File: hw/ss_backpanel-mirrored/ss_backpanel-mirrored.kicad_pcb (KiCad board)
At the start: 2 copper layers, 165 x 51.1 mm, 17 parts, among them J101 4mm_banana_socket-LB_I4R_A-pa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, M101 Amphenol_T3437000-DIN7_panel_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, M102 Amphenol_T3437000-DIN7_panel_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, M103 Mech_cutout_IDC_2x5, M104 FN283-1-06_Schaffner_AC-panel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, M105 74980104400-Wurth_RJ45-Panel_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, M106 TE-1734346-Panel_cutout, M107 CUI-UJ2_AH_1_SMT-Panel_cutout, M109 SJ-3571N_CUI_audio_jacket_pan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, M110 SMA_bulkhead_jack_Panel_cutout, M111 Molex_NanoFit-1x02-Panel_cuto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

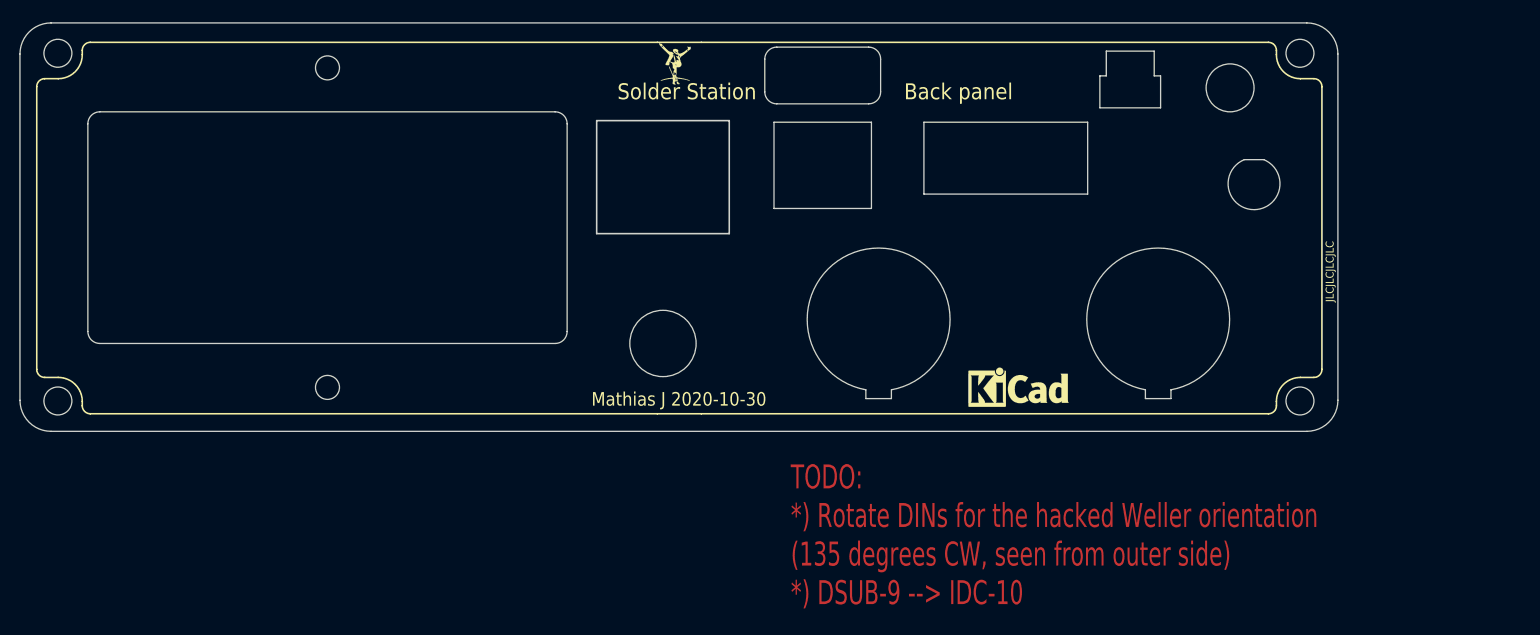
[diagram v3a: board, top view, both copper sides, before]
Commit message: Yet another rear-panel layout shuffle : audio-out to other side; adjust Eth & debug-IDC; align & cleanup
Moving the audio-conn might help confining the audio parts to the rear-right side of MB.
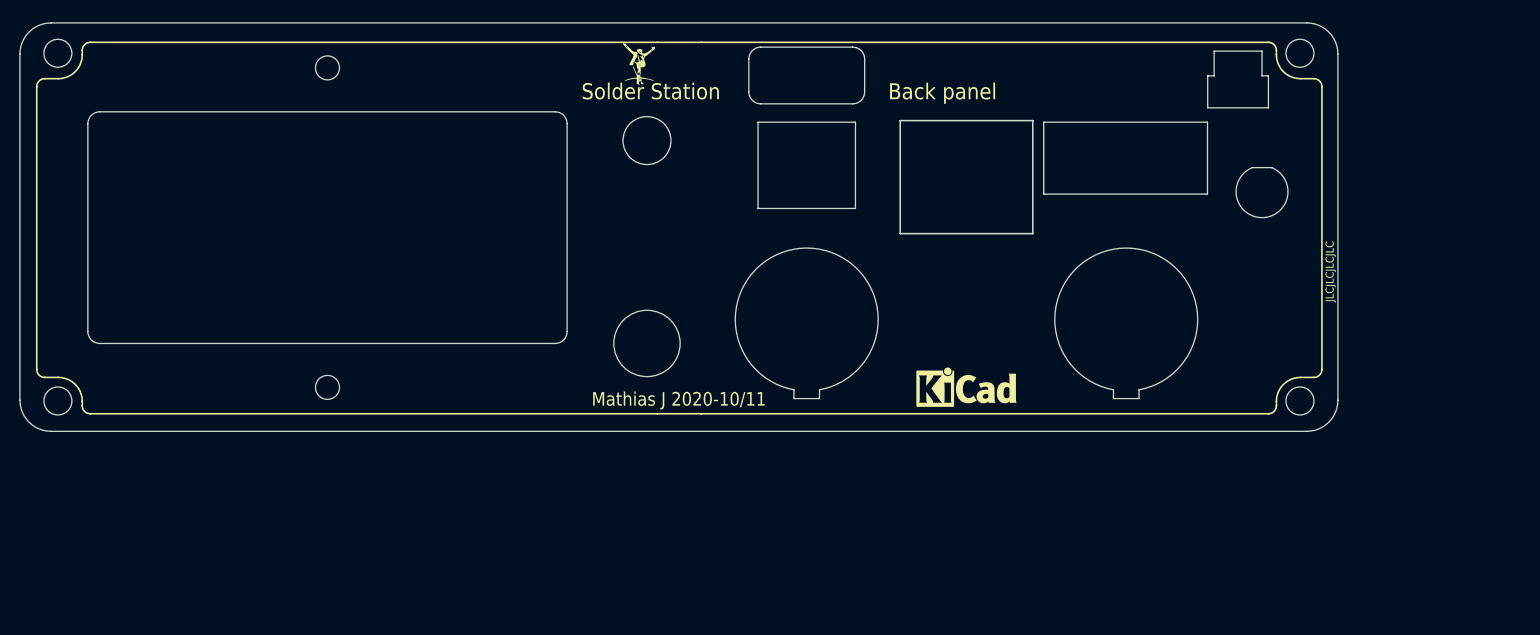
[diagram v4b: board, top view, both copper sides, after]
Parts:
- moved M109 73.0 mm to (146.0, 61.1), turned to 0 degrees
- moved M105 38.0 mm to (186.0, 61.1)
- moved M103 15.0 mm to (205.9, 61.3)
- moved M111 13.5 mm to (220.0, 59.5)
- moved M102 9.00 mm to (166.0, 86.0)
- moved LOGO101 6.50 mm to (186.0, 95.0)
- moved Logo103 4.50 mm to (145.0, 54.0)
- moved M101 4.00 mm to (206.0, 86.0)
- moved J101 2.00 mm to (146.0, 89.0)
- moved M106 2.00 mm to (166.0, 61.1)
- moved M107 2.00 mm to (166.0, 59.5)
- moved M110 1.41 mm to (223.0, 70.0)
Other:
- board text added: "Mathias J 2020-10/11"
- board text removed: "Mathias J 2020-10-30"
- board text removed: "TODO: *) Rotate DINs for the hacked Weller orientation (135 degrees CW, seen from outer side) *) DSUB-9 --> IDC-10"
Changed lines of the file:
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@@
-(kicad_pcb (version 20171130) (host pcbnew 5.1.7-a382d34a8~87~ubuntu18.04.1)
+(kicad_pcb (version 20171130) (host pcbnew 5.1.8-db9833491~87~ubuntu18.04.1)
   (general
     (thickness 1.6)
-    (drawings 49)
+    (drawings 48)
     (tracks 0)
     (zones 0)
@@
   )
   (module customlib_mj_fp:Mech_cutout_IDC_2x5 locked (layer F.Cu)
-    (at 190.92 61.3 180)
+    (at 205.92 61.3 180)
     (descr "Panel cut-out for a right-angled IDC 2x5")
     (tags "IDC 2x5")
@@
   )
   (module customlib_mj_fp:Molex_NanoFit-1x02-Panel_cutout locked (layer B.Cu)
-    (at 206.5 59.5 180)
+    (at 220 59.5 180)
     (descr "Panel cut-out for Molex Nano-Fit 1x02")
     (tags "Molex NanoFit panel cut-out")
@@
     )
   )
-  (module customlib_mj_fp:SMA_Bulkhead_jack-Panel_cutout (layer B.Cu)
-    (at 222 69 90)
+  (module customlib_mj_fp:SMA_Bulkhead_jack-Panel_cutout locked (layer B.Cu)
+    (at 223 70 90)
     (descr "SMA bulkhead jack connector cut-out")
     (tags "SMA panel cutout")
@@
   )
   (module customlib_mj_fp:LB_I4R_A-4mm_banana_socket_panelmnt locked (layer B.Cu)
-    (at 148 89 180)
+    (at 146 89 180)
     (fp_text reference J101 (at 0 5) (layer B.SilkS) hide
       (effects (font (size 1.2 0.8) (thickness 0.16)) (justify mirror))
@@
   )
   (module customlib_mj_fp:CUI-UJ2_AH_1_SMT-Panel_cutout locked (layer B.Cu)
-    (at 168 59.5 180)
+    (at 166 59.5 180)
     (descr "Panel cut-out for CUI-UJ2_AH_1_SMT USB-A host connector")
     (tags "USB-A CUI UJ2_AH_1_SMT panel cut-out")
@@
   )
   (module customlib_mj_fp:SJ-3571N_panel_cutout locked (layer B.Cu)
-    (at 219 59.5 180)
+    (at 146 61.1)
     (descr "Panel cut-out for CUI SJ-3571N 3.5mm audio jack")
     (tags "CUI SJ-3571N 3.5mm audio jack panel cut-out")
@@
       (effects (font (size 1 1) (thickness 0.15)) (justify mirror))
     )
-    (pad "" np_thru_hole circle (at 0 2.5 180) (size 6 6) (drill 6) (layers *.Cu *.Mask))
+    (pad "" np_thru_hole circle (at 0 2.5) (size 6 6) (drill 6) (layers *.Cu *.Mask))
     (model /home/mjoh/projects/stm32/projects/customlib_mj/3d_models/CUI_DEVICES_SJ-3571N.step
       (offset (xyz 0 2.5 0.3))
@@
   )
   (module customlib_mj_fp:74980104400_WE_RJ45_LAN-Panel_cutout locked (layer B.Cu)
-    (at 148 61.1)
+    (at 186 61.1)
     (descr "Panel cut-out for WE RJ45 Ethernet connector")
     (tags "RJ45 panel cut-out")
@@
   )
   (module customlib_mj_fp:TE_1734346-Panel_cutout locked (layer B.Cu)
-    (at 168 61.1)
+    (at 166 61.1)
     (descr "Panel cut-out for TE-1734346 USB-B device connector")
     (tags "USB-B TE-1734346 panel cut-out")
@@
   )
   (module customlib_mj_fp:Amphenol_T3437000-DIN7-panel_cutout locked (layer B.Cu)
-    (at 175 86 180)
+    (at 166 86 180)
     (descr "Amphenol T3437000 DIN7 (Weller connector) panel cutout")
     (tags "Amphenol T3437000 DIN7 panel cutout")
@@
   )
   (module customlib_mj_fp:Amphenol_T3437000-DIN7-panel_cutout locked (layer B.Cu)
-    (at 210 86 180)
+    (at 206 86 180)
     (descr "Amphenol T3437000 DIN7 (Weller connector) panel cutout")
     (tags "Amphenol T3437000 DIN7 panel cutout")
@@
   )
   (module Symbol:KiCad-Logo_5mm_SilkScreen (layer F.Cu)
-    (at 192.5 95)
+    (at 186 95)
     (descr "KiCad Logo")
     (tags "Logo KiCad")
@@
   )
   (module customlib_mj_fp:MJ_Mini (layer F.Cu)
-    (at 149.5 54)
+    (at 145 54)
     (tags "MJ mini")
     (fp_text reference Logo103 (at 0 3.8) (layer F.SilkS) hide
@@
       (xy -1.83067 -2.546882)) (layer F.SilkS) (width 0.01))
   )
-  (gr_text "TODO: \n*) Rotate DINs for the hacked Weller orientation\n(135 degrees CW, seen from outer side)\n*) DSUB-9 --> IDC-10" (at 164 113) (layer F.Cu)
-    (effects (font (size 3 2) (thickness 0.5)) (justify left))
-  )
-  (gr_text "Back panel" (at 185 57.5) (layer F.SilkS)
+  (gr_text "Back panel" (at 183 57.5) (layer F.SilkS)
     (effects (font (size 2 1.8) (thickness 0.4)))
   )
@@
   (gr_line (start 70 59.5) (end 230 59.5) (layer Dwgs.User) (width 0.15))
   (gr_line (start 230 61.1) (end 70 61.1) (layer Dwgs.User) (width 0.15))
-  (gr_text "Solder Station" (at 151 57.5) (layer F.SilkS)
+  (gr_text "Solder Station" (at 146.5 57.5) (layer F.SilkS)
     (effects (font (size 2 1.8) (thickness 0.4)))
   )
-  (gr_text "Mathias J 2020-10-30" (at 150 96) (layer F.SilkS)
+  (gr_text "Mathias J 2020-10/11" (at 150 96) (layer F.SilkS)
     (effects (font (size 1.7 1.5) (thickness 0.3)))
   )

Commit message: Backpanel: added fill zones & labels/icons in silk-screen on back
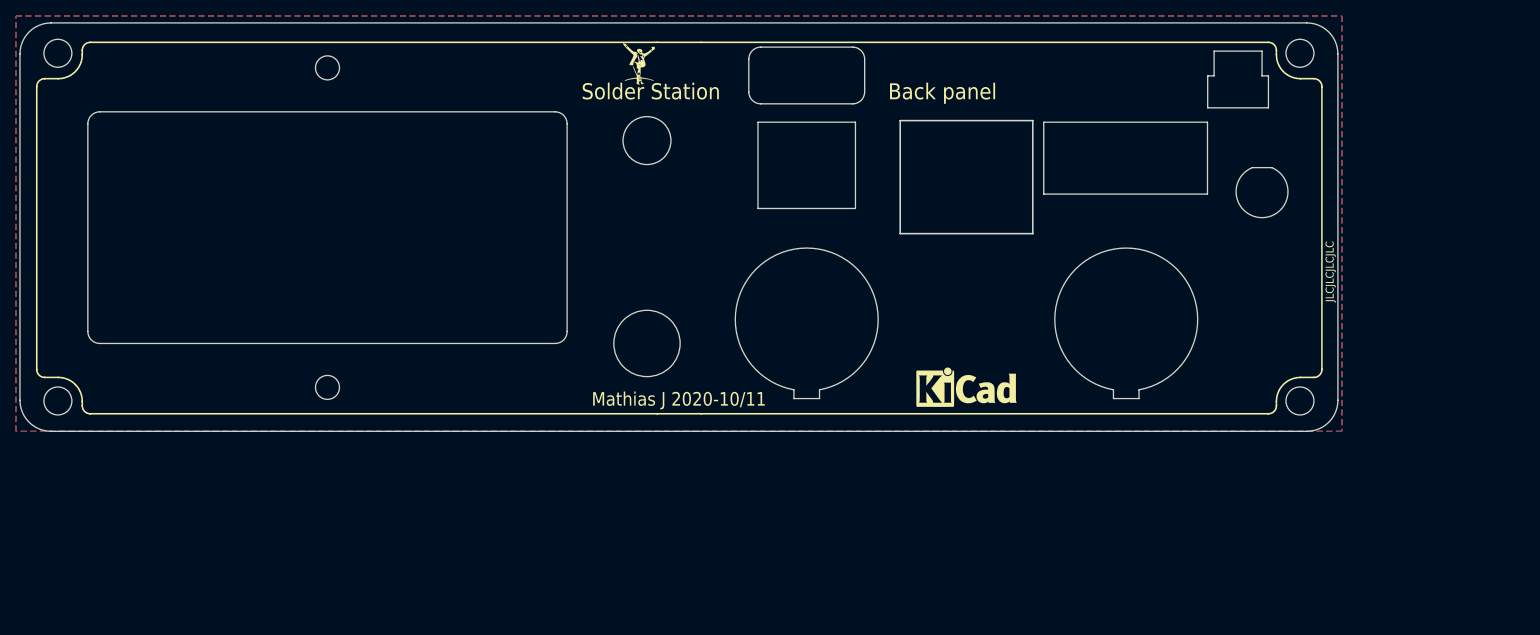
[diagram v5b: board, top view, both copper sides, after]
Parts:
- added G***: LOGO, customlib_mj_fp:ss_logo_fmantenna, B.Cu at (223.0, 76.0)
- added G***: LOGO, customlib_mj_fp:ss_logo_wellercomp, B.Cu at (186.0, 91.0)
- added G***: LOGO, customlib_mj_fp:ss_logo_12Vout, B.Cu at (222.5, 61.0)
- added G***: LOGO, customlib_mj_fp:ss_logo_speakers, B.Cu at (146.0, 68.5)
- added G***: LOGO, customlib_mj_fp:ss_logo_usb, B.Cu at (166.0, 73.5)
- added G***: LOGO, customlib_mj_fp:ss_logo_LAN, B.Cu at (186.0, 79.0)
- added G***: LOGO, customlib_mj_fp:ss_logo_debugconn, B.Cu at (206.0, 72.5)
- added G***: LOGO, customlib_mj_fp:ss_logo_equipotential_symbol, B.Cu at (146.0, 96.5)
- added G***: LOGO, customlib_mj_fp:ss_logo_chan_b, B.Cu at (206.0, 98.0)
- added G***: LOGO, customlib_mj_fp:ss_logo_chan_a, B.Cu at (166.0, 98.0)
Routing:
- added copper zone on B.Cu, net (none)
- added copper zone on F.Cu, net (none)
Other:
- rule pad_to_mask_clearance: 0.05 -> 0

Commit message: Backpanel: Change labels/icons to solder-mask cutout variants instead (for e.g. ENIG on black)
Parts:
- G***: footprint customlib_mj_fp:ss_logo_equipotential_symbol -> customlib_mj_fp:ss_logo_equipotential_symbol-f_mask
- G***: footprint customlib_mj_fp:ss_logo_fmantenna -> customlib_mj_fp:ss_logo_fmantenna-f_mask
- G***: footprint customlib_mj_fp:ss_logo_speakers -> customlib_mj_fp:ss_logo_speakers-f_mask
- G***: footprint customlib_mj_fp:ss_logo_chan_a -> customlib_mj_fp:ss_logo_chan_a-f_mask
- G***: footprint customlib_mj_fp:ss_logo_usb -> customlib_mj_fp:ss_logo_usb-f_mask
- G***: footprint customlib_mj_fp:ss_logo_LAN -> customlib_mj_fp:ss_logo_LAN-f_mask
- G***: footprint customlib_mj_fp:ss_logo_wellercomp -> customlib_mj_fp:ss_logo_wellercomp-f_mask
- G***: footprint customlib_mj_fp:ss_logo_chan_b -> customlib_mj_fp:ss_logo_chan_b-f_mask
- G***: footprint customlib_mj_fp:ss_logo_debugconn -> customlib_mj_fp:ss_logo_debugconn-f_mask
- G***: footprint customlib_mj_fp:ss_logo_12Vout -> customlib_mj_fp:ss_logo_12Vout-f_mask

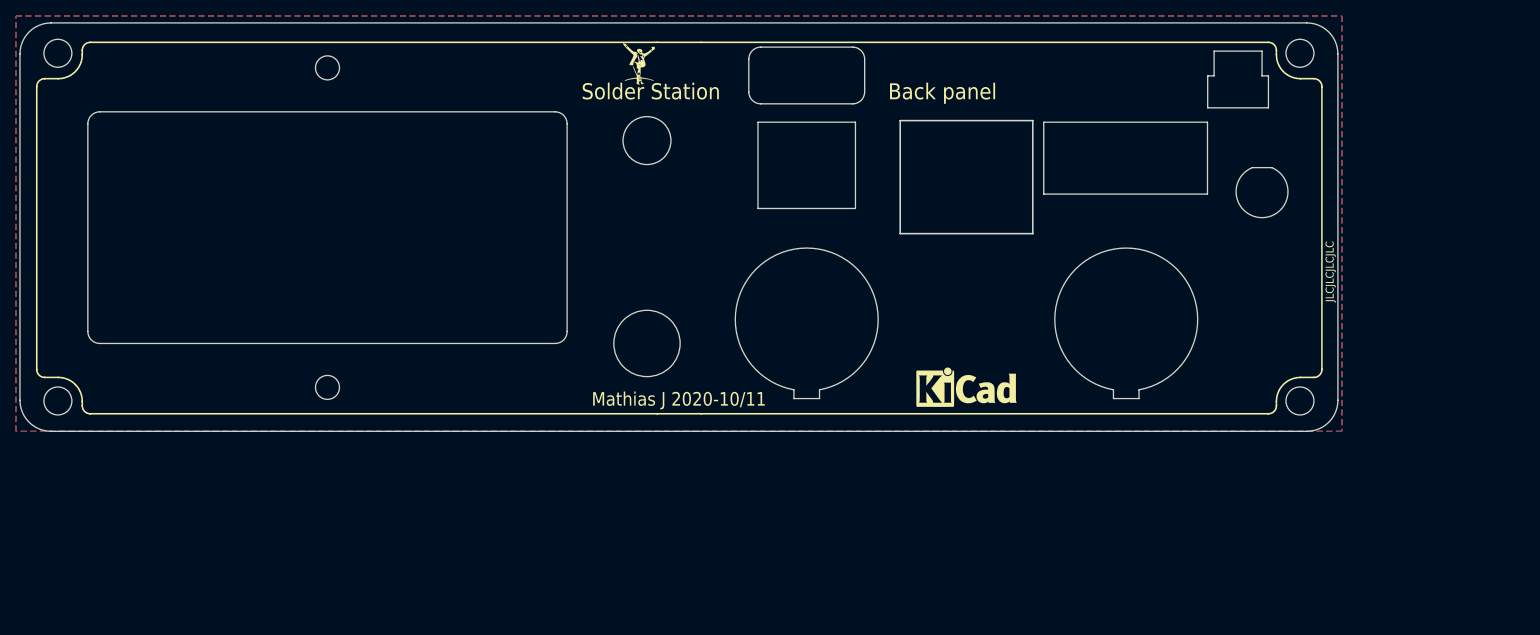
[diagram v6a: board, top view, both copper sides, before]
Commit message: Backpanel (solder-mask labels) : Remove Cu-fill on inside. Keep all-board fill on outside for now (KISS)
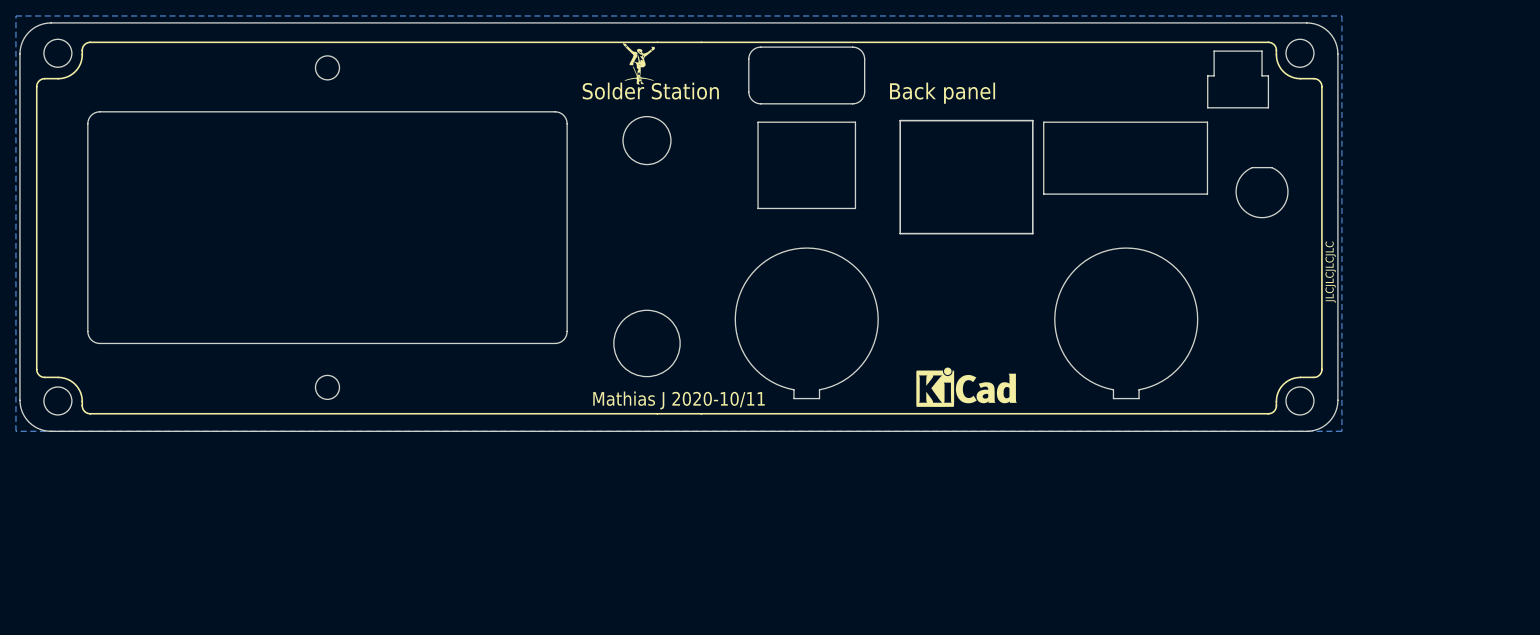
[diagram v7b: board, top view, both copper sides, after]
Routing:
- removed copper zone on F.Cu, net (none)
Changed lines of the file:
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@@
   (gr_line (start 67.5 96.11) (end 67.5 52.76) (angle 90) (layer Edge.Cuts) (width 0.05))
   (gr_arc (start 71.39 52.76) (end 71.39 48.87) (angle -90) (layer Edge.Cuts) (width 0.05))
-  (zone (net 0) (net_name "") (layer F.Cu) (hatch edge 0.508)
-    (connect_pads (clearance 0.2))
-    (min_thickness 0.154)
-    (fill yes (arc_segments 32) (thermal_gap 0.508) (thermal_bridge_width 0.508))
-    (polygon
-      (pts
-        (xy 233 100) (xy 67 100) (xy 67 48) (xy 233 48)
-      )
-    )
-  )
   (zone (net 0) (net_name "") (layer B.Cu) (hatch edge 0.508)
     (connect_pads (clearance 0))

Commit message: Backpanel (solder-mask labels) : Also remove label 'Weller-compatible' to reduce clutter
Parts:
- removed the G*** at (186.0, 91.0)
